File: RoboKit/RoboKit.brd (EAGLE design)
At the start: 134 x 82 mm, 32 parts, among them CON1 XT30UPB-M, CON2 XT30UPB-M, P1 B6B-PH-K, P2 B6B-PH-K, U1 SSM6J808R, X3 JST-XH-02-PIN-LONG-PAD, X4 JST-XH-02-PIN-LONG-PAD, X5 JST-XH-04-PIN-LONG-PAD, X6 JST-XH-04-PIN-LONG-PAD, X7 JST-XH-10-PIN-LONG-PAD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

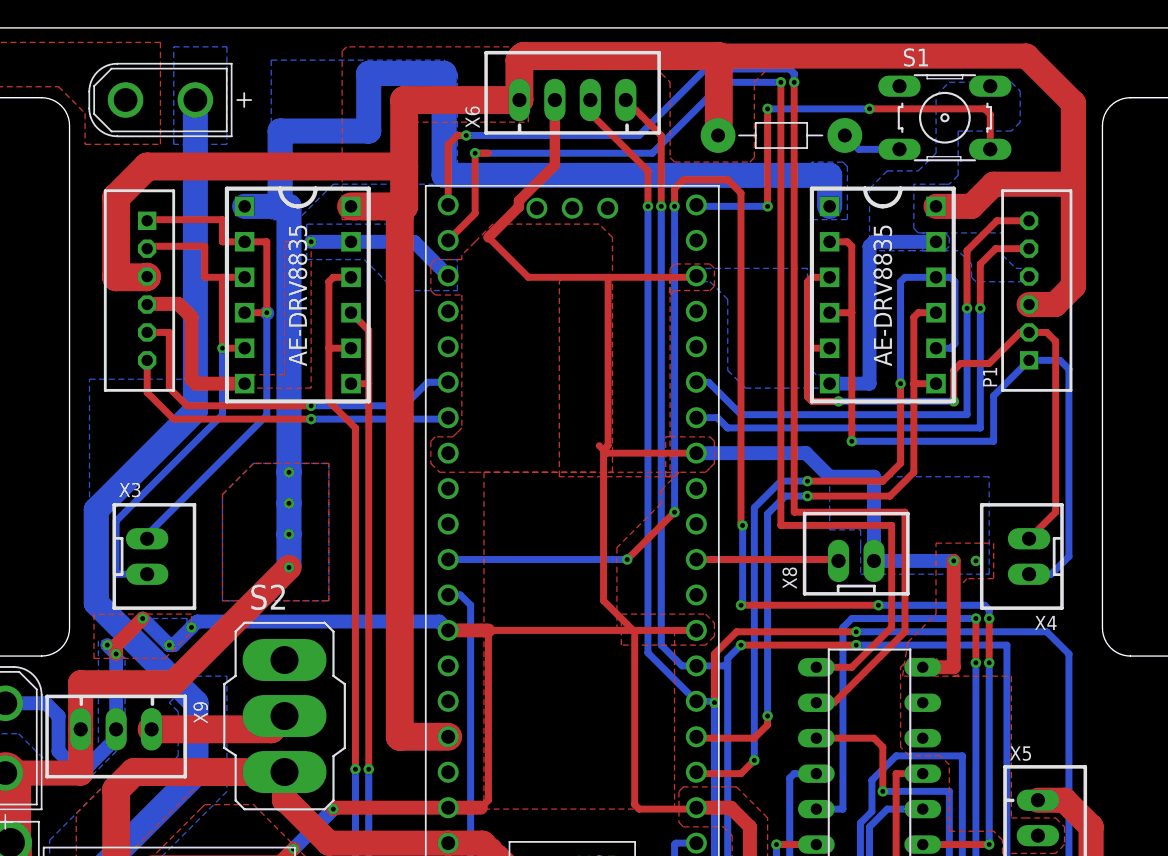
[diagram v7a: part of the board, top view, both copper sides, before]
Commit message: モーター部分の太さを修正
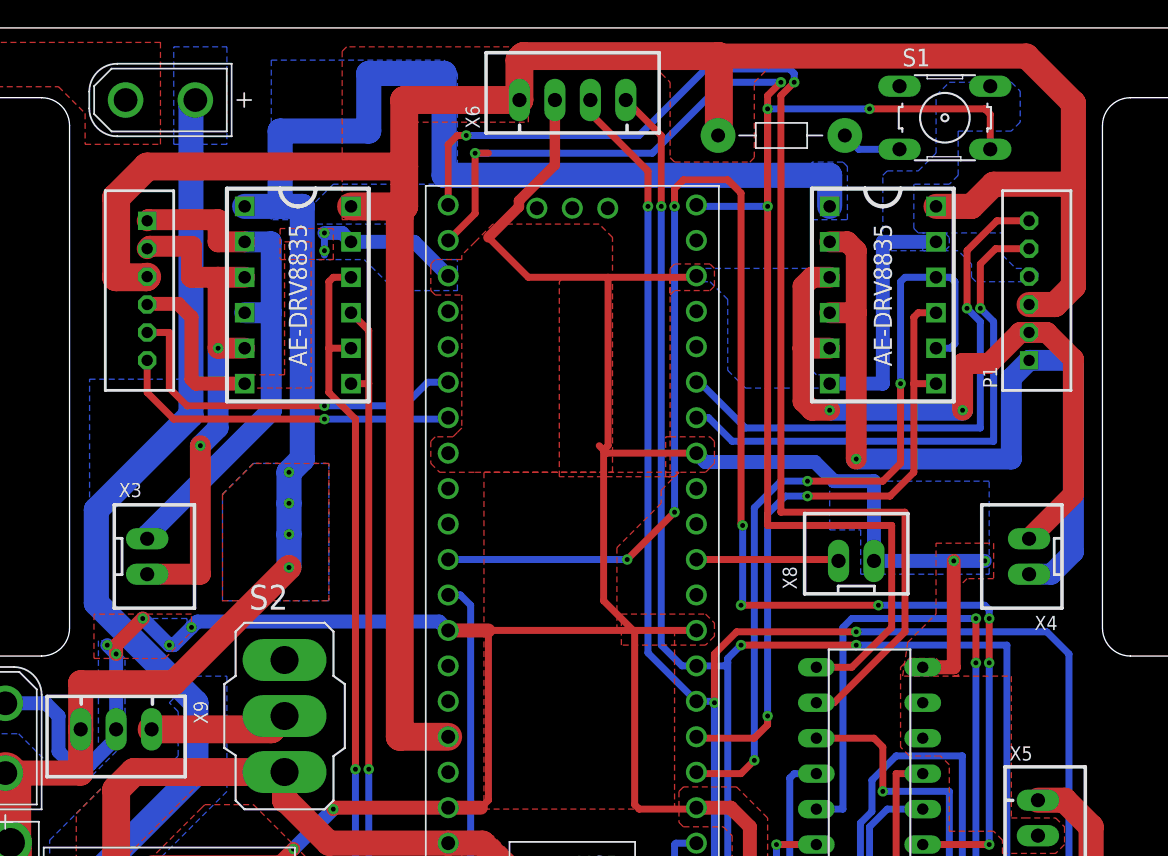
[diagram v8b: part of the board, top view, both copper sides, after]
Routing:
- net MOTOR_A_R: track 54.2 -> 58.4 mm
- net MOTOR_B_R: track 48.0 -> 51.2 mm
- net GND: track 293.2 -> 296.3 mm, vias 11 -> 13
- net HALL_A_R: track 36.3 -> 39.0 mm
- net HALL_B_R: track 37.4 -> 40.1 mm
- net VOUT: track 176.3 -> 177.6 mm
- net B: track 85.6 -> 86.9 mm
- net A: track 87.9 -> 89.2 mm
- net MOTOR_A_L: track 36.7 -> 37.4 mm, vias 1 -> 0
- net MOTOR_B_L: track 37.5 -> 36.8 mm, vias 1 -> 2
